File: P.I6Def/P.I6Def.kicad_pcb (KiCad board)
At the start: 2 copper layers, 46.1 x 52.7 mm, 42 parts, among them J1 B3B-PH-K-S, J2 B3B-PH-K-S, J3 CX90B-16P1, J4 B4B-PH-SM4-TB_LF__SN__P_, J5 B4B-PH-SM4-TB_LF__SN__P_, SW2 SW_SPST, SW3 SW_SPST, U2 LMV321IDCKT, U3 LMV321IDCKT, U4 LMV321IDCKT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

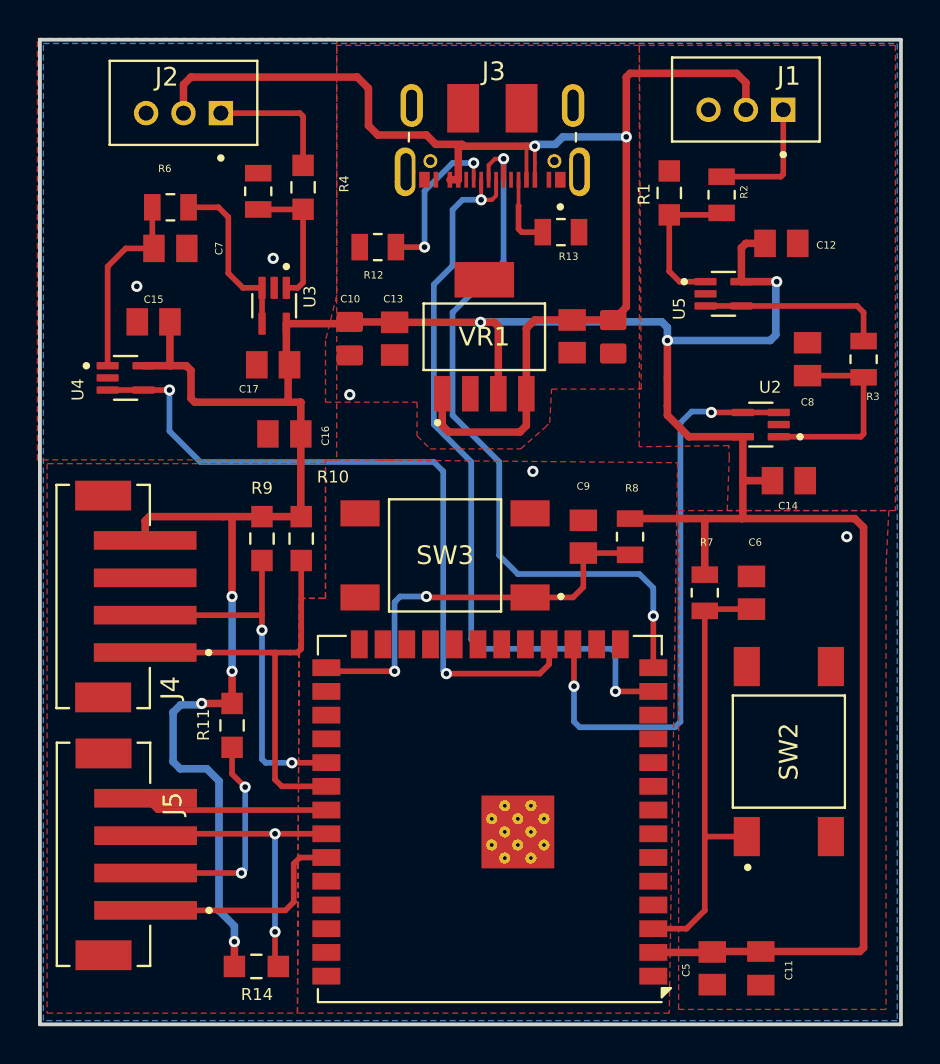
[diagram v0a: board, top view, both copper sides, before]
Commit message: Correcciones planos de tierra
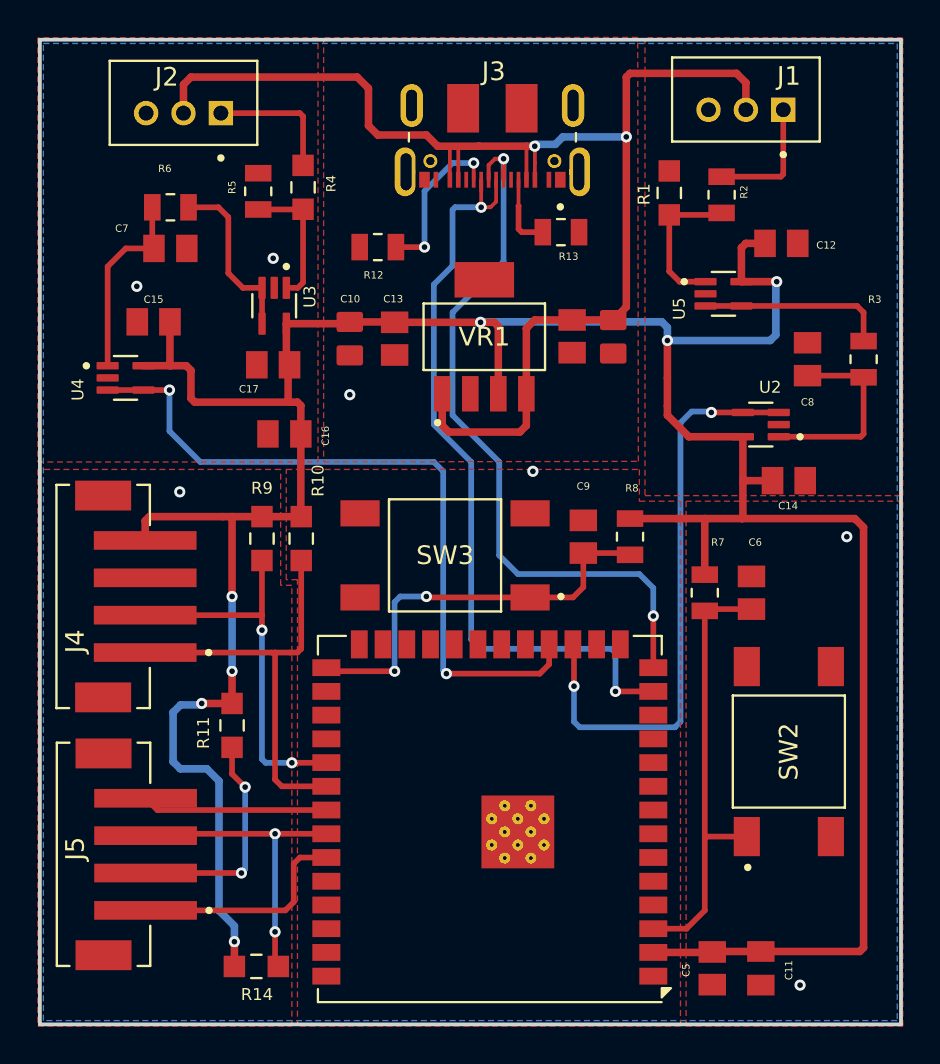
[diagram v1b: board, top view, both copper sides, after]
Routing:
- net +5V: track 72.1 -> 73.5 mm
- net /D-: track 41.6 -> 42.1 mm
- net GND: vias 5 -> 7

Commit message: Creacion de archivos gerber
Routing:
- net /D-: track 42.1 -> 41.5 mm
- net GND: vias 7 -> 29
